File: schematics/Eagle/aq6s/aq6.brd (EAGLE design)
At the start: 99.8 x 66.8 mm, 26 parts

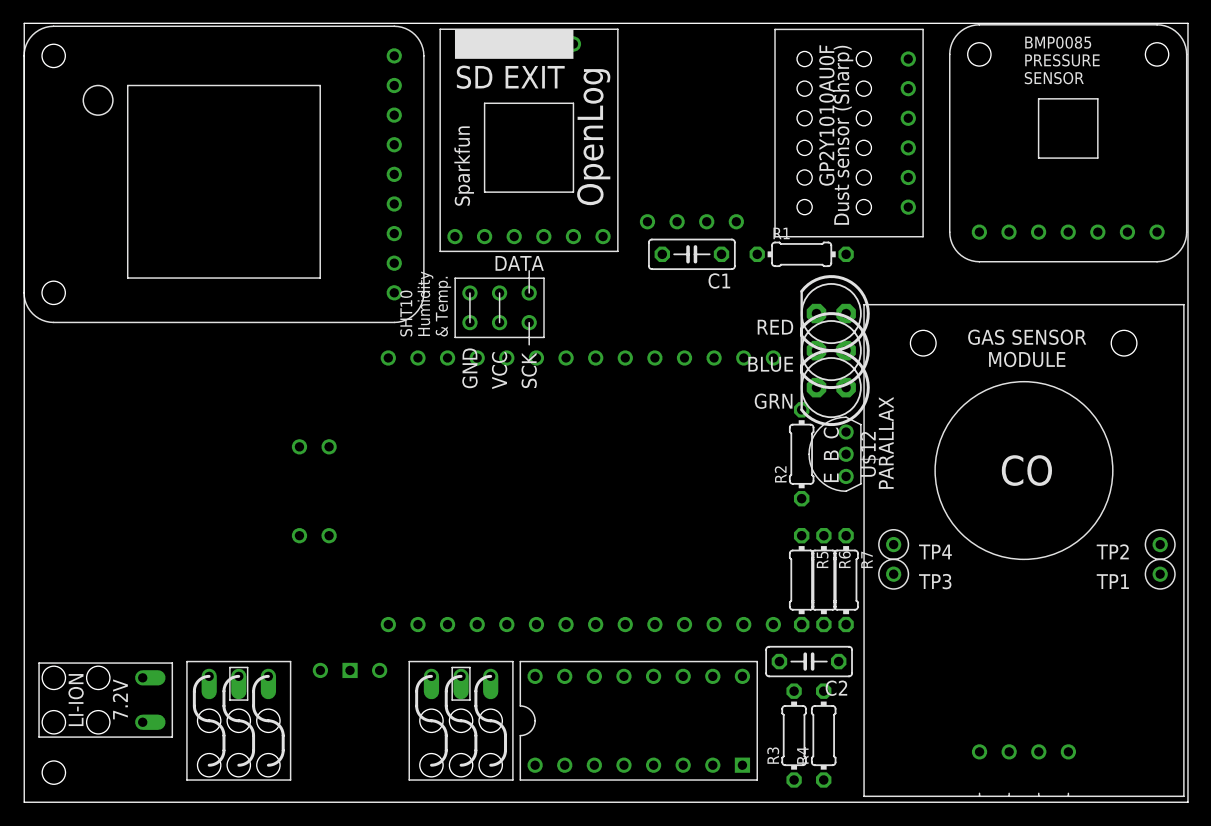
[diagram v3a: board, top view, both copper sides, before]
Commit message: PCB first draft, needs checking and adjustment
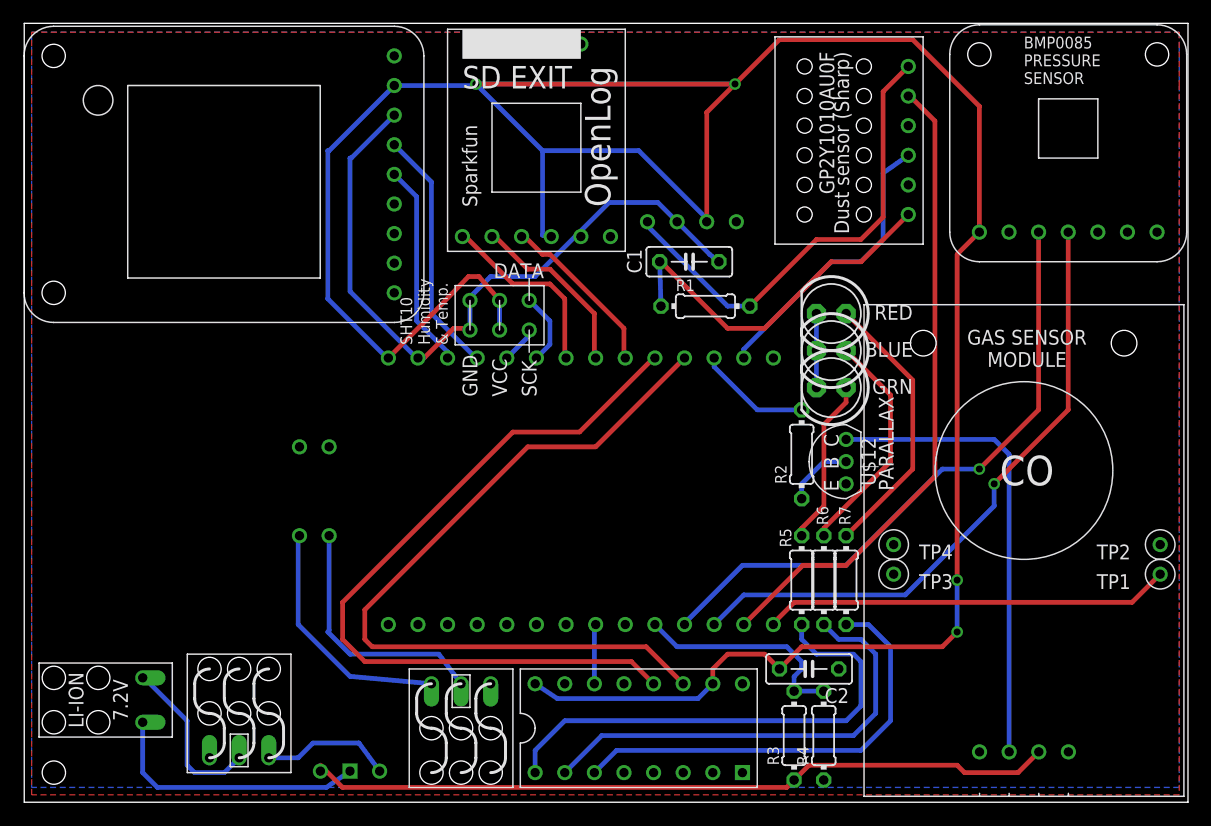
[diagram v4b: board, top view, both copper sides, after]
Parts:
- moved U$7 14.3 mm to (32.4, 1.40), turned to 0 degrees
- moved U$11 10.8 mm to (21.0, 2.54), turned to 180 degrees
- moved R1 9.38 mm to (58.4, 42.5)
- moved C1 0.67 mm to (57.0, 46.4), turned to 0 degrees
- moved U$1 0.64 mm to (70.7, 56.8)
- moved U$5 0.64 mm to (36.3, 47.2)
- moved U$9 0.64 mm to (51.4, 7.62)
- moved C2 0.63 mm to (67.3, 11.4)
- moved U$10 0.63 mm to (34.9, 11.4)
- moved U$12 0.63 mm to (70.5, 29.2)
- moved U$6 0.63 mm to (40.8, 41.8)
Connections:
- net GND: now also U$9.P$13
- net N$12: now also U$2.D4; no longer U$2.D13
- net N$13: now also U$2.D5*; no longer U$2.D11*
- net N$17: now also U$2.D11*; no longer U$2.D5*
- net N$21: now also U$2.A3; no longer U$2.A1
- net N$22: now also U$2.A1; no longer U$2.A2
- net N$23: now also U$2.A4; no longer U$2.A5
- net N$24: now also U$2.A5; no longer U$2.A4
- net N$25: now also U$9.P$1; no longer U$9.P$15
- net N$26: now also U$2.D10; no longer U$2.D9*
- net N$27: now also U$2.D9*; no longer U$2.D10
- net N$28: now also U$9.P$3; no longer U$9.P$2
- net N$29: now also U$9.P$2; no longer U$9.P$1
- net N$7: now also U$2.D6*; no longer U$2.D8
- net N$9: now also U$2.D8; no longer U$2.D6*
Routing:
- net 3V3: track 0.00 -> 252.5 mm, vias 0 -> 4
- net N$26: track 0.00 -> 67.8 mm
- net GND: track 0.00 -> 66.9 mm
- net N$27: track 0.00 -> 66.9 mm
- net N$18: track 0.00 -> 64.7 mm
- net N$3: track 0.00 -> 55.3 mm
- net N$24: track 0.00 -> 54.4 mm, vias 0 -> 1
- net N$23: track 0.00 -> 53.3 mm, vias 0 -> 1
- net N$25: track 0.00 -> 42.4 mm
- net 5V: track 0.00 -> 40.4 mm
- net N$19: track 0.00 -> 40.0 mm
- net N$29: track 0.00 -> 39.4 mm
- net N$28: track 0.00 -> 38.2 mm
- net N$20: track 0.00 -> 35.0 mm
- net N$2: track 0.00 -> 31.5 mm
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- added copper zone on layer 1, net GND
- added copper zone on layer 16, net GND

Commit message: Removed mux/bit shift register
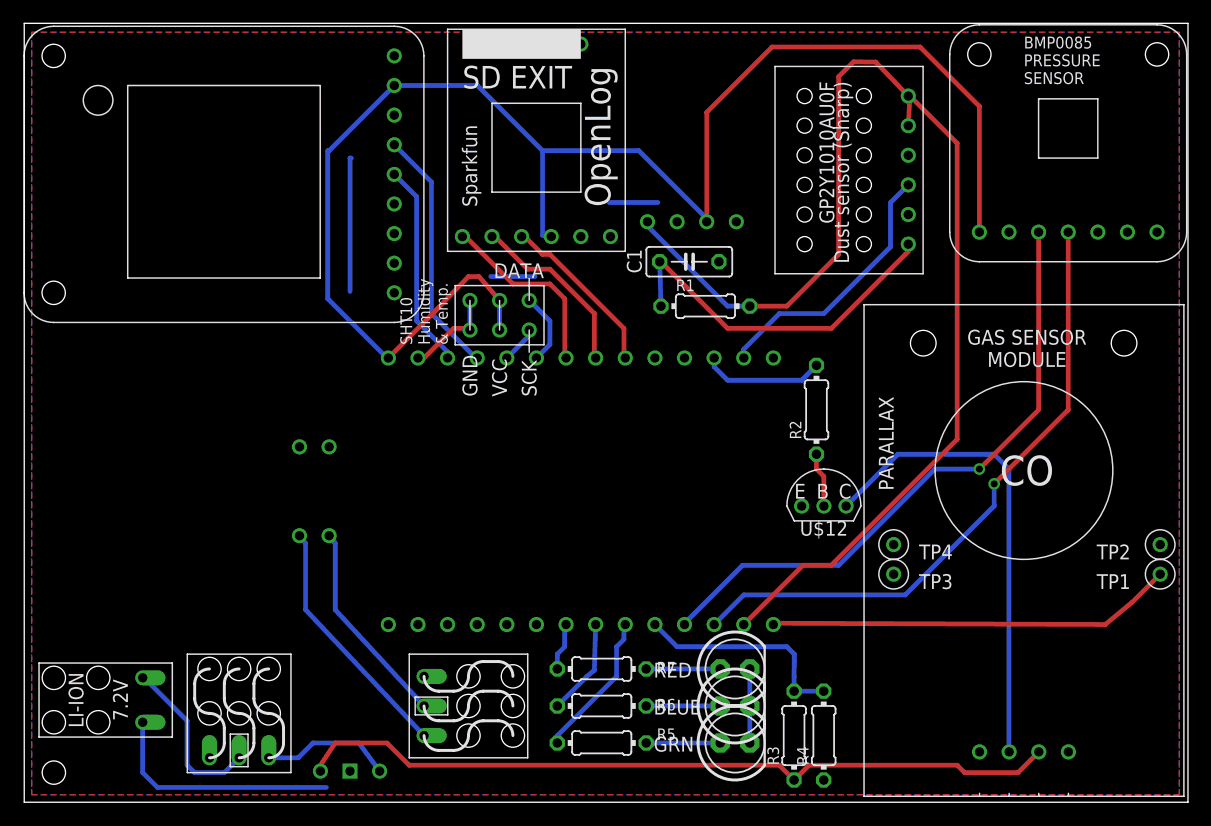
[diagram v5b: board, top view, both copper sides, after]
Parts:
- removed C2: 1 uF, resistor:C050-025X075
- removed U$9: M74HC595B1, air_quality_parts:16DIP
- moved GRN 31.6 mm to (61.0, 5.08), turned to 0 degrees
- moved BLUE 31.6 mm to (61.0, 8.26), turned to 0 degrees
- moved RED 31.6 mm to (61.0, 11.4), turned to 0 degrees
- moved R7 22.3 mm to (49.5, 11.4), turned to 180 degrees
- moved R5 22.1 mm to (49.5, 5.08), turned to 180 degrees
- moved R6 21.9 mm to (49.5, 8.26), turned to 180 degrees
- moved U$10 6.02 mm to (33.0, 5.71), turned to 90 degrees
- moved U$12 4.26 mm to (68.6, 25.4), turned to 0 degrees
- moved R2 4.02 mm to (67.9, 33.7)
- moved U$1 2.54 mm to (70.7, 54.2)
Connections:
- removed net N$22: U$2.A1, U$9.P$14
- removed net N$25: R5.2, U$9.P$1
- net 3V3: no longer C2.2, U$9.P$10, U$9.P$16
- net GND: now also LI-ION.GND, U$2.GND@E, U$7.GND; no longer C2.1, U$9.P$13
- net N$15: now also R5.2, U$2.A2; no longer LI-ION.GND, U$7.GND
- net N$26: no longer U$9.P$11
- net N$27: no longer U$9.P$12
- net N$28: now also U$2.A0; no longer U$9.P$3
- net N$29: now also U$2.A1; no longer U$9.P$2
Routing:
- net 3V3: track 252.5 -> 131.7 mm, vias 4 -> 0
- net N$26: track 67.8 -> 0.00 mm
- net N$27: track 66.9 -> 0.00 mm
- net N$25: track 42.4 -> 0.00 mm
- net N$28: track 38.2 -> 4.12 mm
- net N$29: track 39.4 -> 8.34 mm
- net N$30: track 23.8 -> 6.35 mm
- net N$31: track 19.8 -> 6.35 mm
- net GND: track 66.9 -> 55.3 mm
- net N$15: track 23.1 -> 12.6 mm
- net N$32: track 14.3 -> 6.35 mm
- net N$22: track 5.13 -> 0.00 mm
- net 5V: track 40.4 -> 44.4 mm
- net N$10: track 21.8 -> 17.8 mm
- net N$3: track 55.3 -> 58.5 mm
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
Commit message: Thickened pcd traces
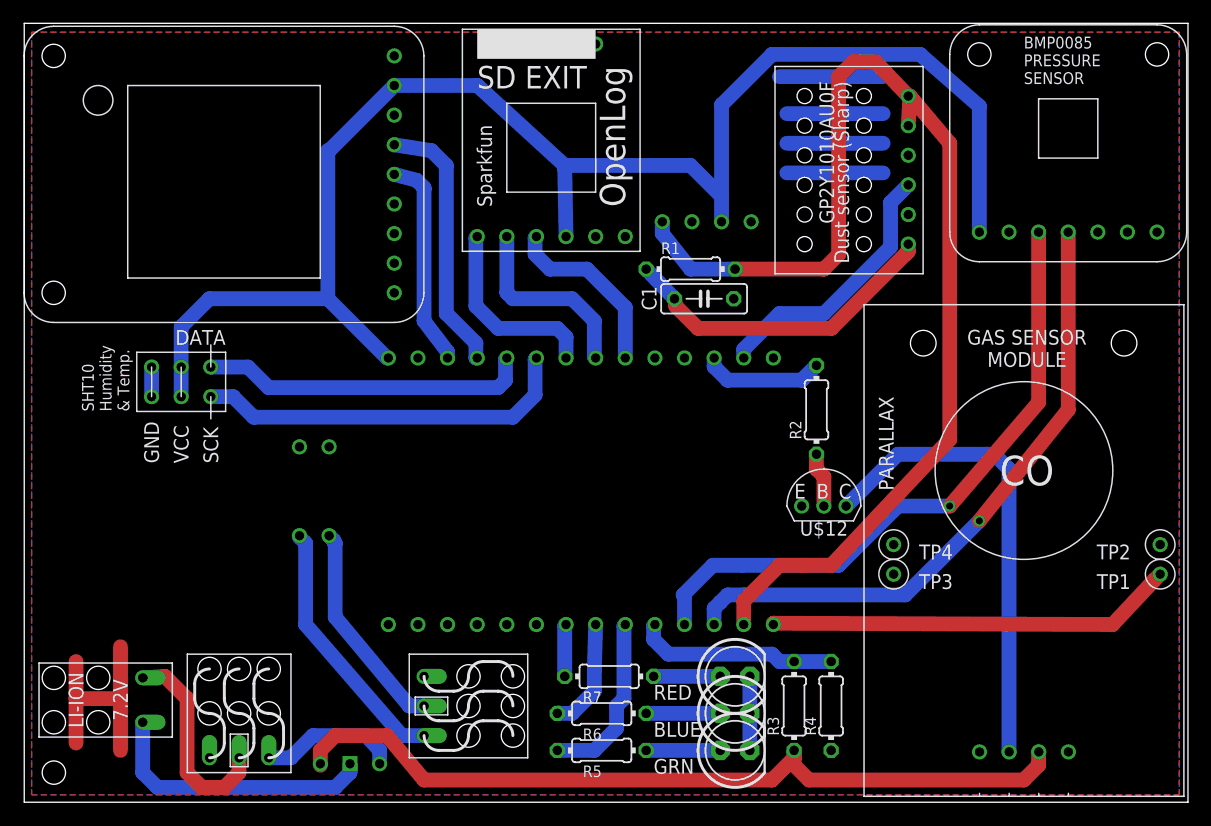
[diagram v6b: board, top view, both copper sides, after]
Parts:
- moved U$6 27.9 mm to (13.5, 36.1)
- moved C1 3.42 mm to (58.3, 43.2)
- moved R1 3.42 mm to (57.1, 45.7)
- moved R4 2.62 mm to (69.2, 8.26)
- moved R3 2.54 mm to (66.0, 8.26)
- moved U$3 1.27 mm to (58.5, 56.1)
- moved U$5 1.27 mm to (37.6, 47.2)
- moved R7 0.90 mm to (50.2, 10.8)
- moved BLUE 0.64 mm to (61.0, 7.62)
- moved R6 0.64 mm to (49.5, 7.62)
- moved U$7 0.64 mm to (32.4, 2.03)
- moved GRN 0.63 mm to (61.0, 4.45)
- moved R5 0.63 mm to (49.5, 4.45)
- moved RED 0.63 mm to (61.0, 10.8)
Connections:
- net N$12: now also U$2.D5*; no longer U$2.D4
- net N$13: now also U$2.D4; no longer U$2.D5*
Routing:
- net GND: track 55.3 -> 86.1 mm
- net N$12: track 3.19 -> 32.6 mm
- net N$13: track 6.16 -> 28.2 mm
- net N$18: track 66.0 -> 70.1 mm
- net N$11: track 14.4 -> 17.7 mm, vias 0 -> 1
- net 5V: track 44.4 -> 41.1 mm
- net N$2: track 30.9 -> 28.2 mm
- net N$15: track 12.6 -> 15.1 mm
- net N$23: track 53.3 -> 54.9 mm
- net N$4: track 21.3 -> 22.7 mm
- net N$21: track 18.7 -> 17.3 mm
- net N$29: track 8.34 -> 9.68 mm
- net N$8: track 15.4 -> 16.5 mm
- net N$6: track 21.4 -> 22.3 mm
- net N$9: track 14.6 -> 15.5 mm
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
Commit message: pcb images
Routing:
- net GND: track 86.1 -> 62.9 mm
- net N$24: track 54.7 -> 56.5 mm
- net N$1: track 22.9 -> 23.5 mm
